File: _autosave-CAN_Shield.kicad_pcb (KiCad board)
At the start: 2 copper layers, 65 x 56 mm, 20 parts, among them J1 GPIO, U1 MX128-5.08-09P-GN01-CU-Y-A, U2 MCP2515T-I/SO, U4 SN65HVD230DR, X1 X322516MLB4SI

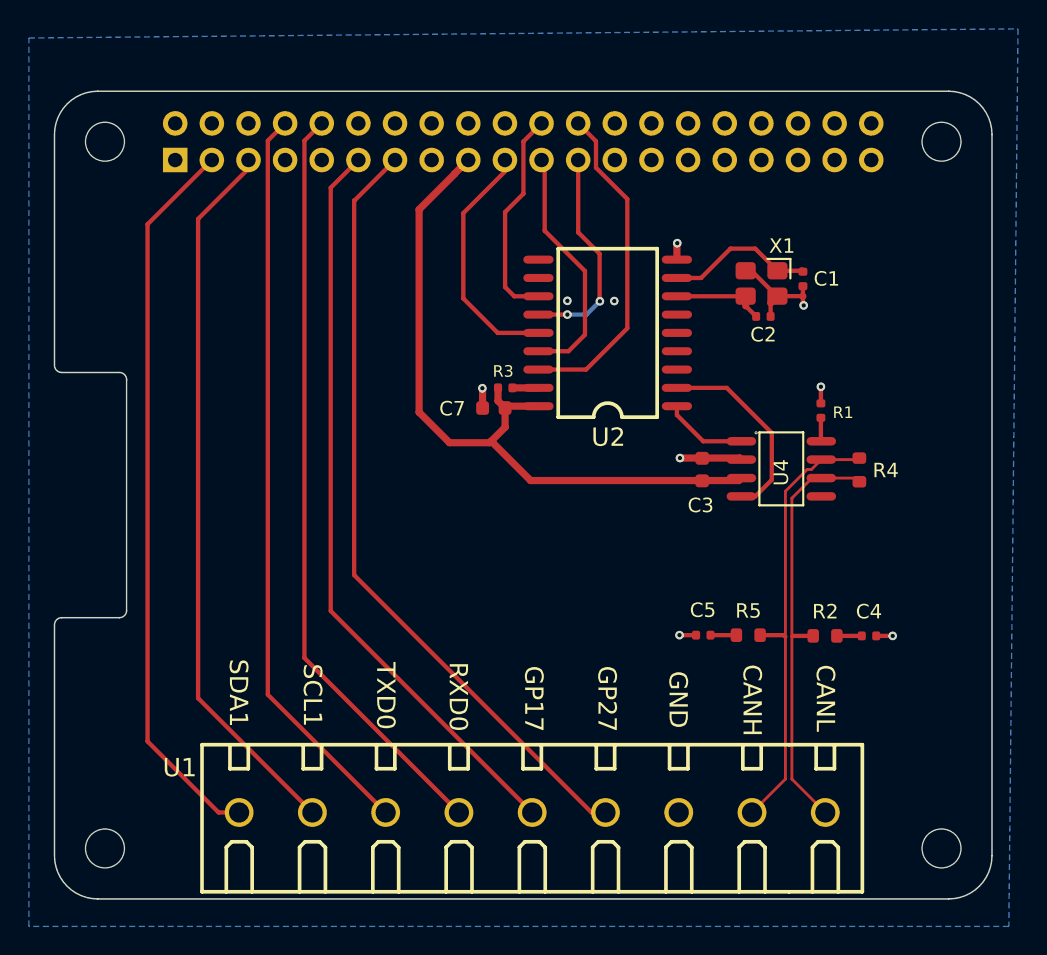
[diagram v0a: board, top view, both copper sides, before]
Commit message: remove transfer via and fix erc: logo silk screen
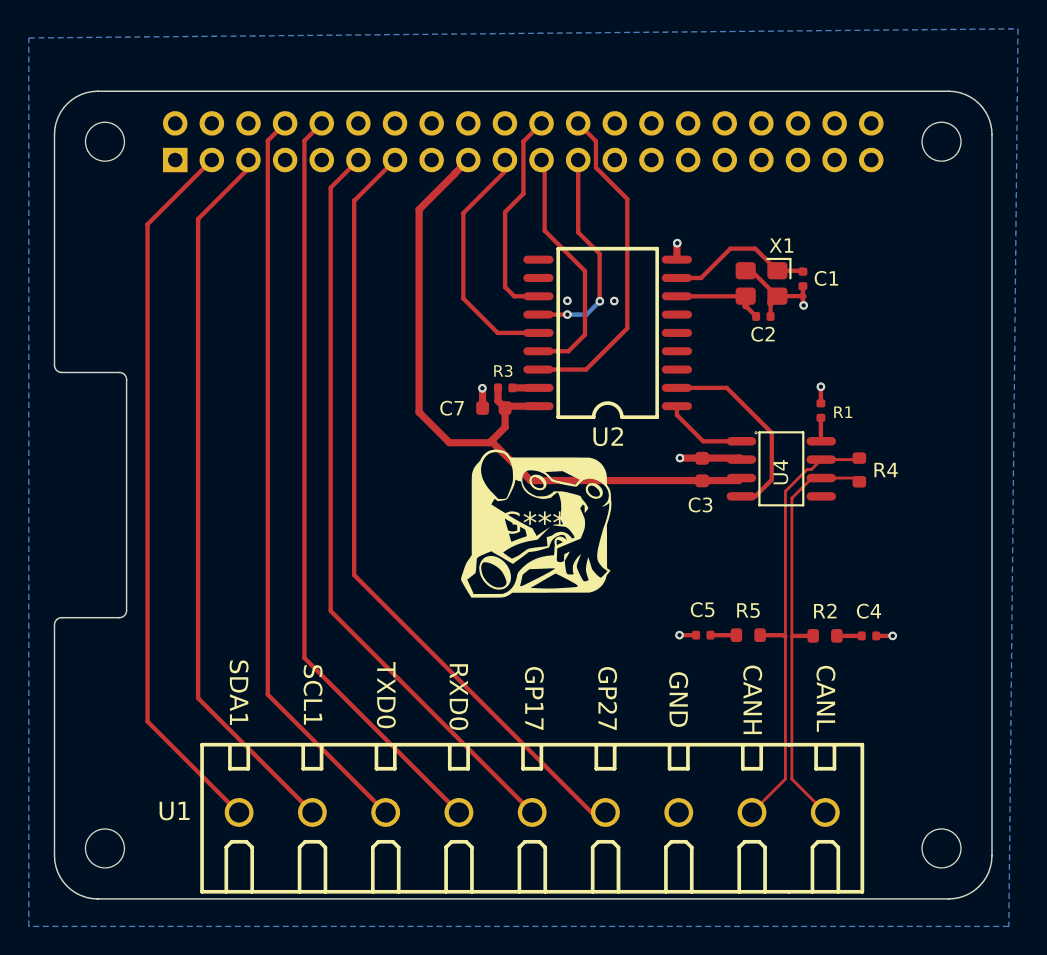
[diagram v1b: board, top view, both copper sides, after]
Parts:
- added G***: LOGO, LOGO, F.Cu at (133.2, 74.0)
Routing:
- net /GPIO2/SDA1: track 50.5 -> 49.7 mm

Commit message: extend pcb edge for smt header by double click the line and change from User.Drawing to Edgecuts
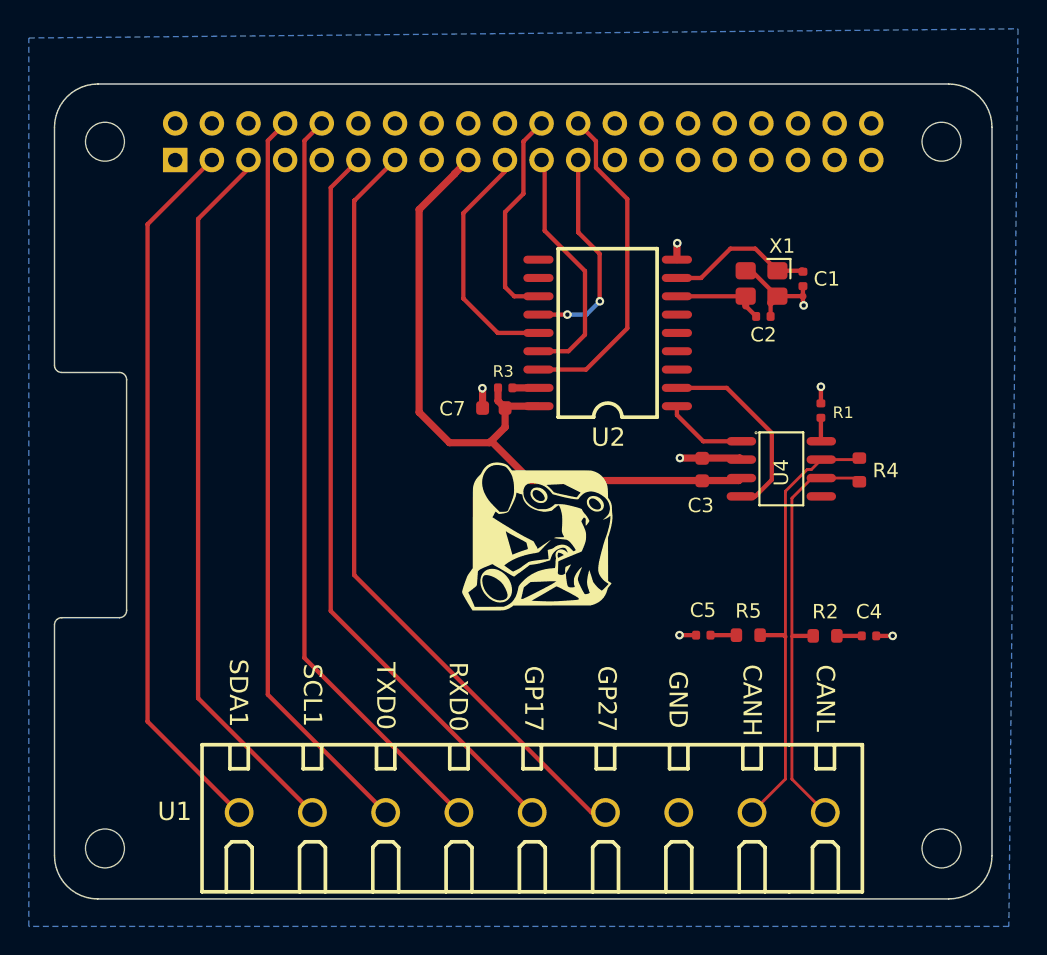
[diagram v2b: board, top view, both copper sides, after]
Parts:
- moved G*** 0.89 mm to (133.3, 74.9)
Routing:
- net GND: vias 9 -> 7
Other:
- board size 65 x 56 mm -> 65 x 56.5 mm
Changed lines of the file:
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@@
 	(footprint "LOGO"
 		(layer "F.Cu")
-		(at 133.200343 73.964499)
+		(at 133.274 74.854)
 		(property "Reference" "G***"
-			(at 0 0 0)
+			(at 0.067601 0.576794 0)
 			(layer "F.SilkS")
+			(hide yes)
 			(effects
 				(font
@@
 		)
 	)
-	(gr_line
-		(start 162 43.5)
-		(end 103 43.5)
-		(stroke
-			(width 0.1)
-			(type solid)
-		)
-		(layer "Dwgs.User")
-	)
 	(gr_rect
 		(start 166 81.825)
@@
 		(layer "Dwgs.User")
 	)
+	(gr_line
+		(start 100 63)
+		(end 100 81)
+		(stroke
+			(width 0.1)
+			(type solid)
+		)
+		(layer "Dwgs.User")
+	)
+	(gr_line
+		(start 100 47)
+		(end 100 46.5)
+		(stroke
+			(width 0.1)
+			(type solid)
+		)
+		(layer "Dwgs.User")
+	)
+	(gr_rect
+		(start 169.9 46.355925)
+		(end 187 59.455925)
+		(locked yes)
+		(stroke
+			(width 0.1)
+			(type solid)
+		)
+		(fill none)
+		(layer "Dwgs.User")
+	)
+	(gr_line
+		(start 162 43.5)
+		(end 103 43.5)
+		(stroke
+			(width 0.1)
+			(type solid)
+		)
+		(layer "Edge.Cuts")
+	)
+	(gr_arc
+		(start 100.5 63.5)
+		(mid 100.146447 63.353553)
+		(end 100 63)
+		(stroke
+			(width 0.1)
+			(type solid)
+		)
+		(layer "Edge.Cuts")
+	)
+	(gr_line
+		(start 165 97)
+		(end 165 46.5)
+		(stroke
+			(width 0.1)
+			(type solid)
+		)
+		(layer "Edge.Cuts")
+	)
+	(gr_line
+		(start 100 46.5)
+		(end 100 63)
+		(stroke
+			(width 0.1)
+			(type solid)
+		)
+		(layer "Edge.Cuts")
+	)
 	(gr_arc
 		(start 100 46.5)
@@
 			(type solid)
 		)
-		(layer "Dwgs.User")
-	)
-	(gr_line
-		(start 100 63)
-		(end 100 81)
-		(stroke
-			(width 0.1)
-			(type solid)
-		)
-		(layer "Dwgs.User")
-	)
-	(gr_line
-		(start 100 47)
-		(end 100 46.5)
-		(stroke
-			(width 0.1)
-			(type solid)
-		)
-		(layer "Dwgs.User")
-	)
-	(gr_rect
-		(start 169.9 46.355925)
-		(end 187 59.455925)
-		(locked yes)
-		(stroke
-			(width 0.1)
-			(type solid)
-		)
-		(fill none)
-		(layer "Dwgs.User")
+		(layer "Edge.Cuts")
 	)
 	(gr_arc
@@
 			(type solid)
 		)
-		(layer "Dwgs.User")
-	)
-	(gr_arc
-		(start 100.5 63.5)
-		(mid 100.146447 63.353553)
-		(end 100 63)
-		(stroke
-			(width 0.1)
-			(type solid)
-		)
-		(layer "Edge.Cuts")
-	)
-	(gr_arc
-		(start 162 44)
-		(mid 164.12132 44.87868)
-		(end 165 47)
-		(stroke
-			(width 0.1)
-			(type solid)
-		)
-		(layer "Edge.Cuts")
-	)
-	(gr_line
-		(start 165 97)
-		(end 165 47)
-		(stroke
-			(width 0.1)
-			(type solid)
-		)
-		(layer "Edge.Cuts")
-	)
-	(gr_line
-		(start 100 47)
-		(end 100 63)
-		(stroke
-			(width 0.1)
-			(type solid)
-		)
 		(layer "Edge.Cuts")
 	)
@@
 		(layer "Edge.Cuts")
 	)
-	(gr_arc
-		(start 100 47)
-		(mid 100.87868 44.87868)
-		(end 103 44)
-		(stroke
-			(width 0.1)
-			(type solid)
-		)
-		(layer "Edge.Cuts")
-	)
 	(gr_line
 		(start 100 81)
@@
 		(layer "Edge.Cuts")
 	)
-	(gr_line
-		(start 162 44)
-		(end 103 44)
-		(stroke
-			(width 0.1)
-			(type solid)
-		)
-		(layer "Edge.Cuts")
-	)
 	(gr_text "RXD0"
 		(at 127.9908 85.9792 270)
@@
 	)
 	(via
-		(at 138.8112 58.5472)
-		(size 0.6)
-		(drill 0.3)
-		(layers "F.Cu" "B.Cu")
-		(net 1)
-	)
-	(via
 		(at 143.18 54.534)
 		(size 0.6)
@@
 		(size 0.6)
 		(drill 0.3)
-		(layers "F.Cu" "B.Cu")
-		(net 1)
-	)
-	(via
-		(at 135.56 58.53)
-		(size 0.6)
-		(drill 0.3)

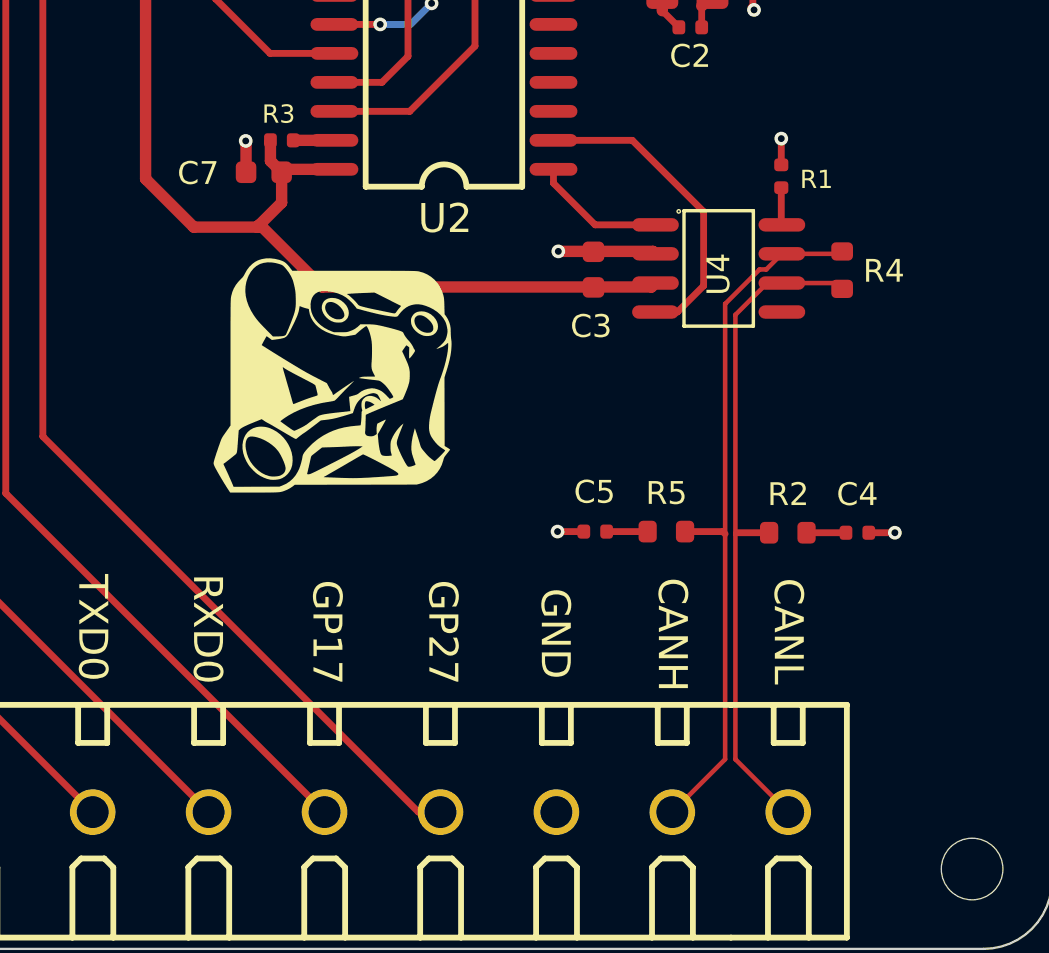
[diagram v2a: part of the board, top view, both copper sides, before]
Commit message: change can diff pair trace width to 0.35 mm get 133ohm zdiff
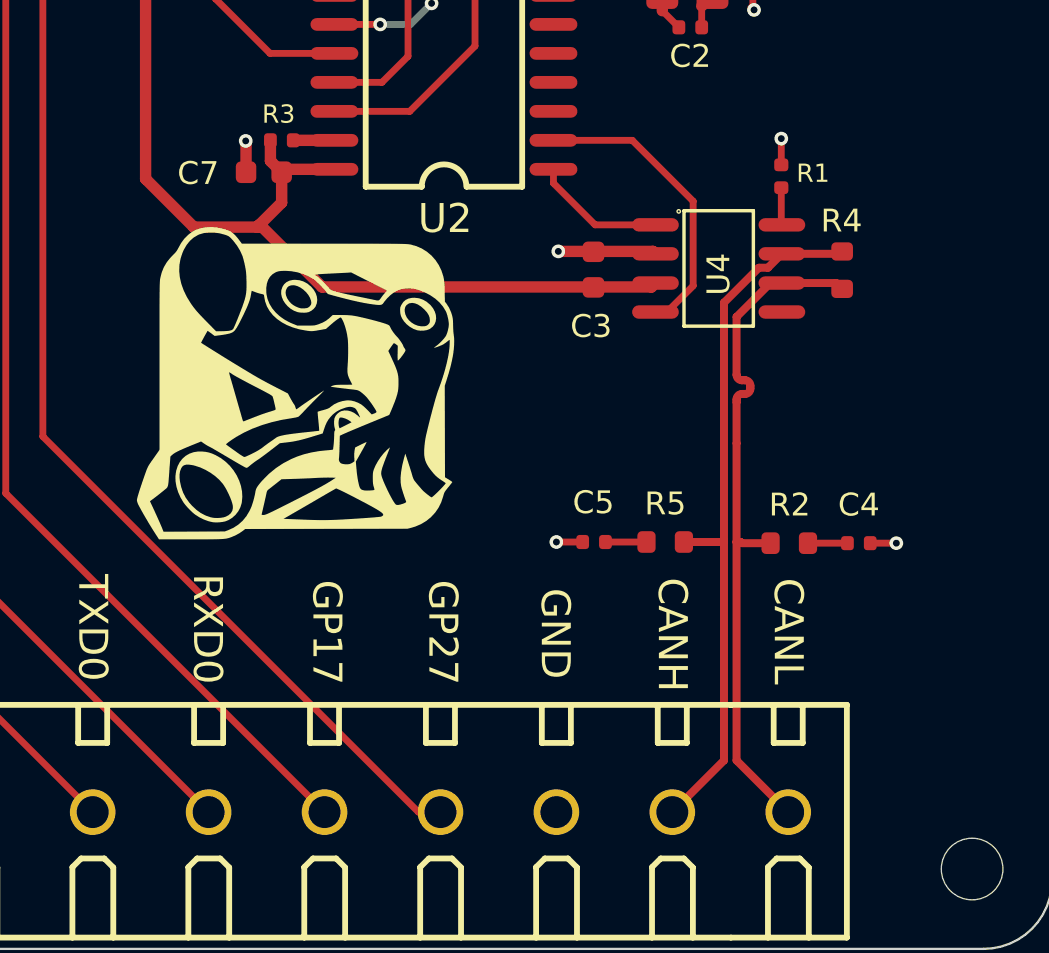
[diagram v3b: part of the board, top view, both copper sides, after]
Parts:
- moved G*** 1.72 mm to (131.6, 75.2)
- moved C4 0.46 mm to (156.5, 82.2)
- moved R2 0.46 mm to (153.5, 82.2)
- moved R5 0.46 mm to (148.0, 82.2)
- moved C5 0.46 mm to (144.9, 82.2)
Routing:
- net /CAN_D-: track 29.5 -> 30.3 mm
- net /RXCAN: track 13.7 -> 13.1 mm
